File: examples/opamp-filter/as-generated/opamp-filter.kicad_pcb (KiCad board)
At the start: 2 copper layers, 80 x 45 mm, 19 parts, among them J1 IN, J2 5V, J3 OUT, U1 MCP6001R, U2 MCP6001R

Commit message: Regenerate the five as round three drew them
All five reviewed projects pass their gates again: the buck all wire
with its feedback drawn home, the motor's logic named at the header,
the carrier reading as the pinout table it is - with its feed diode
finally pointing the right way - the filter compact with test points,
and the FPGA's capacitors sitting beside the units they feed. Thirty
renders redrawn, verdict tables at today's numbers.

Co-Authored-By: Claude Fable 5 <noreply@anthropic.com>
Claude-Session: https://claude.ai/code/session_01DUj7Ltu92tWg159mCSacwY
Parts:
- added TP1: TP, TestPoint:TestPoint_Pad_D1.5mm, F.Cu at (140.2, 73.8)
- added TP2: TP, TestPoint:TestPoint_Pad_D1.5mm, F.Cu at (156.2, 83.8)
- added TP3: TP, TestPoint:TestPoint_Pad_D1.5mm, F.Cu at (146.2, 97.8)
- moved J2 40.0 mm to (130.2, 67.8)
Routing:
- net GND: track 65.3 -> 88.9 mm
- net /VREF: track 64.1 -> 80.2 mm
- net /OUT: track 40.0 -> 46.1 mm
- net /FILT_IN: track 16.5 -> 21.8 mm
- net +5V: track 106.3 -> 108.7 mm
- net /MID: track 24.6 -> 23.7 mm
- net /IN_DC: track 21.7 -> 22.4 mm

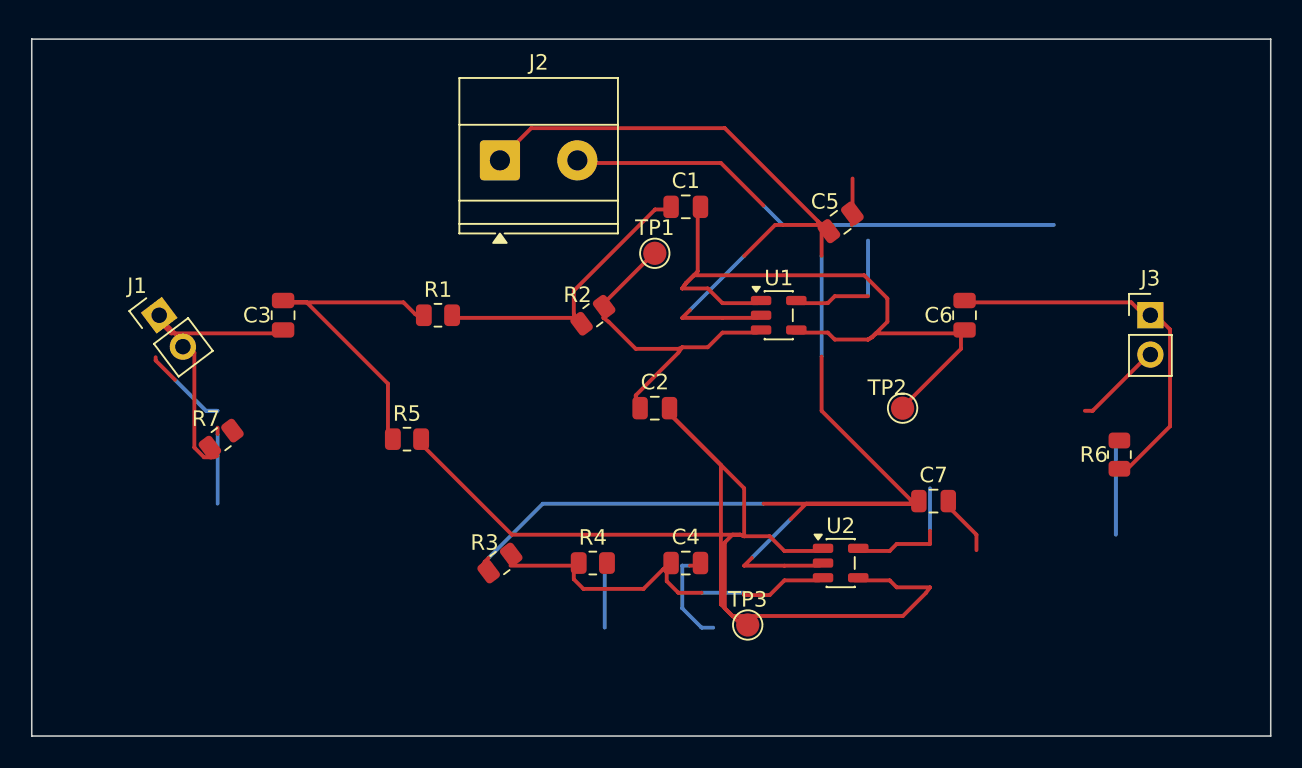
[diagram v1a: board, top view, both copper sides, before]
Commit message: Regenerate the four boards round four has settled
The buck, the motor driver, the carrier and the filter as the current
generator draws them: interior ground stitching on all four, the motor
driver's bundle tight and its board twelve millimetres shorter, the
filter compact and hand-placed, the carrier's indicator in a column of
its own. All four pass their gates. The FPGA is still regenerating.

Co-Authored-By: Claude Fable 5 <noreply@anthropic.com>
Claude-Session: https://claude.ai/code/session_01DUj7Ltu92tWg159mCSacwY
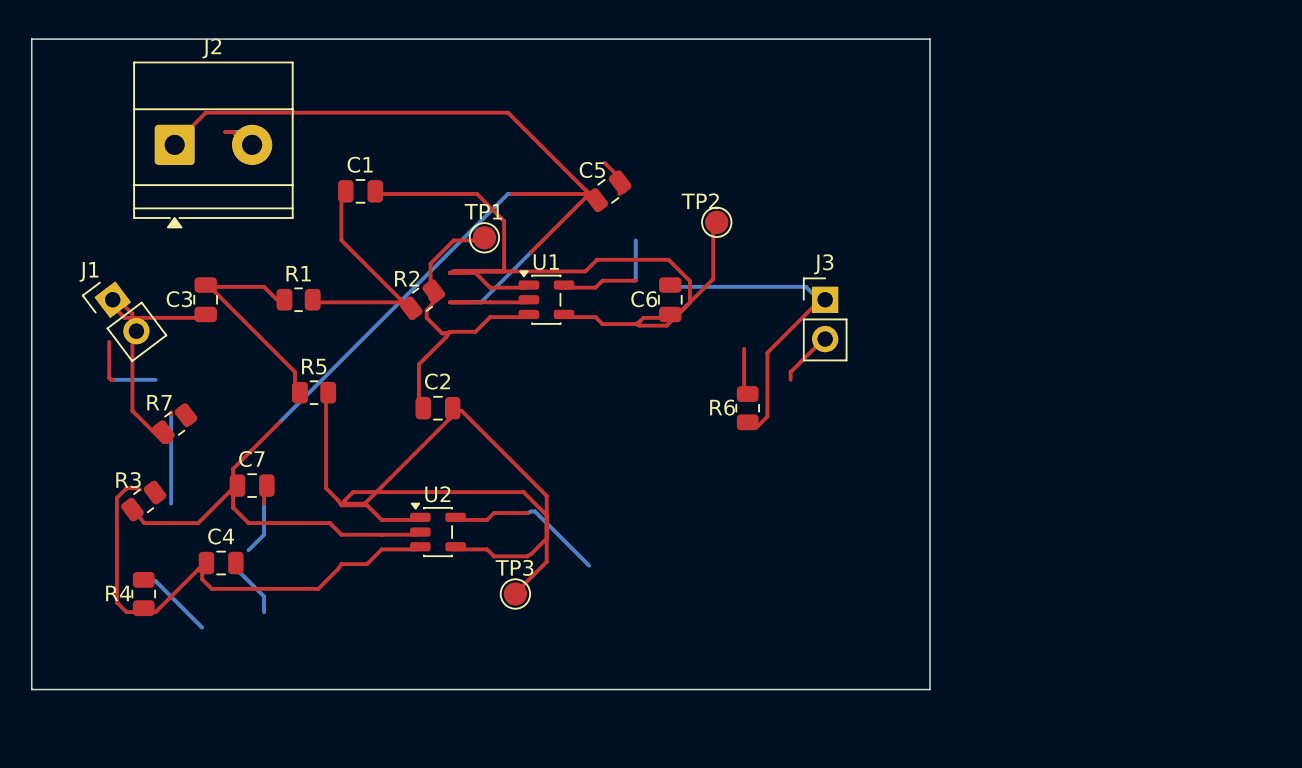
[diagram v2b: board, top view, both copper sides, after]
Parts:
- moved C7 44.0 mm to (114.2, 88.8)
- moved C4 30.0 mm to (112.2, 93.8)
- moved R4 29.1 mm to (107.2, 95.8), turned to 90 degrees
- moved U2 26.1 mm to (126.2, 91.8)
- moved R6 24.2 mm to (146.2, 83.8)
- moved R3 23.3 mm to (107.2, 89.8)
- moved J3 21.0 mm to (151.2, 76.8)
- moved C1 21.0 mm to (121.2, 69.8)
- moved J2 21.0 mm to (109.2, 66.8)
- moved C6 19.0 mm to (141.2, 76.8)
- moved TP2 17.0 mm to (144.2, 71.8)
- moved C5 15.1 mm to (137.2, 69.8)
- moved TP3 15.1 mm to (131.2, 95.8)
- moved U1 15.0 mm to (133.2, 76.8)
- moved C2 14.0 mm to (126.2, 83.8)
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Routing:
- net GND: track 88.9 -> 55.2 mm
- net /VREF: track 80.2 -> 61.1 mm
- net /OUT: track 46.1 -> 58.0 mm
- net +5V: track 108.7 -> 99.6 mm
- net /MID: track 23.7 -> 31.7 mm
- net /IN_DC: track 22.4 -> 15.3 mm
- net /OUT_AC: track 25.2 -> 21.2 mm
- net /X: track 18.2 -> 14.9 mm
- net /IN: track 19.7 -> 17.8 mm
- net /FILT_IN: track 21.8 -> 20.7 mm
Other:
- board size 80 x 45 mm -> 58 x 42 mm

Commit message: Regenerate the four boards whose corners were off the grid
Ninety-one bends at angles nobody chose, now none. All four still pass
their gates.

Co-Authored-By: Claude Fable 5 <noreply@anthropic.com>
Claude-Session: https://claude.ai/code/session_01DUj7Ltu92tWg159mCSacwY
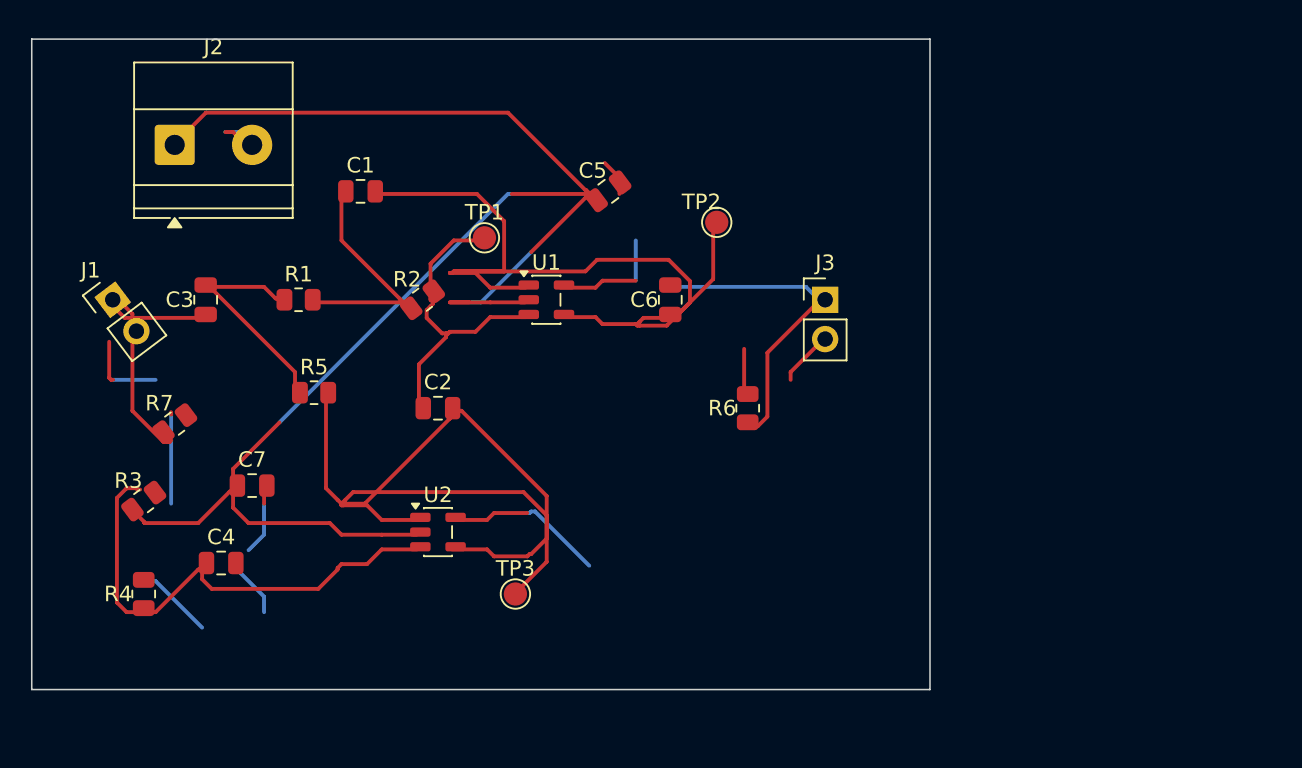
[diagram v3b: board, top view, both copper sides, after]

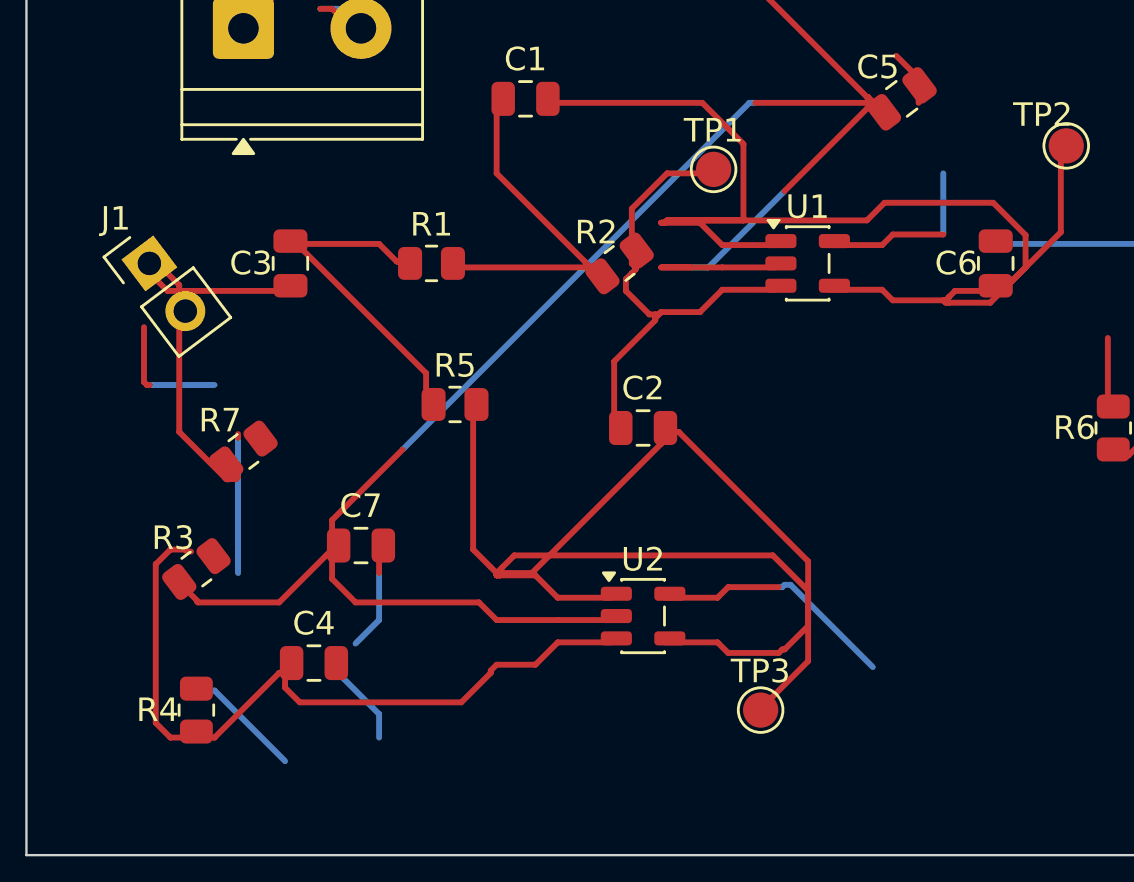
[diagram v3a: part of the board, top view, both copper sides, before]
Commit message: Regenerate the four the text and width work changed
Designators and values off the rails they were printed on, power-named
nets at the width their rule asks for, and the buck's feedback ending
on the capacitor pad it senses at.

Co-Authored-By: Claude Fable 5 <noreply@anthropic.com>
Claude-Session: https://claude.ai/code/session_01DUj7Ltu92tWg159mCSacwY
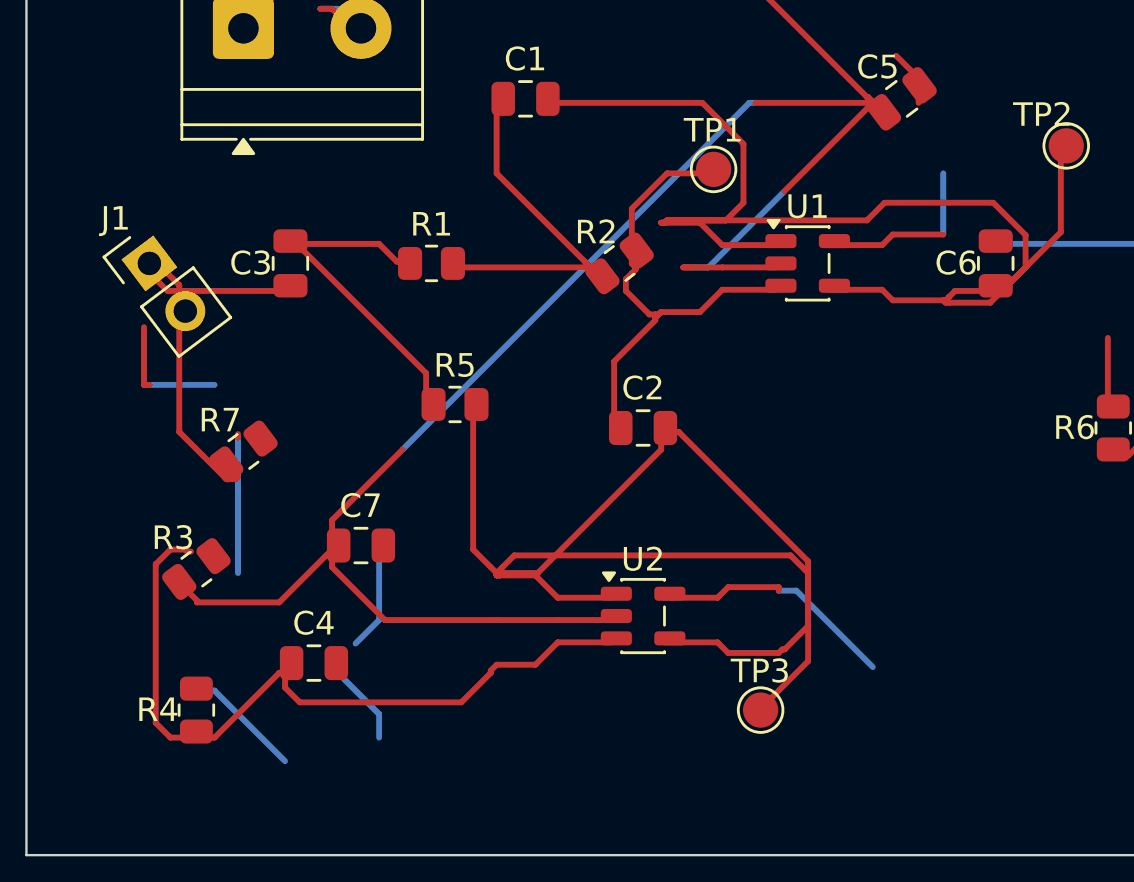
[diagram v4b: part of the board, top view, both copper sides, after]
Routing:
- net +5V: track 99.6 -> 97.5 mm
- net /IN: track 17.9 -> 17.0 mm
- net /VREF: track 61.2 -> 61.8 mm
